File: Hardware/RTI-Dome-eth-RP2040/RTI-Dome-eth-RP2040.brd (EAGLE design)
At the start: 106.7 x 71.2 mm, 112 parts, among them IC1 RP2040, IC2 24LC128T-I_SN, IC3 FT232RL, IC5 74LVC245, IC6 74ABT245, IC7 W25Q128JVSIM_TR, IC8 REG1117-3.3V, IC9 REG1117-5V, J1 47642-1001, J2 XT60PW-M, U1 W5500, X13 PN61729-S, X9 J1011F21PNL

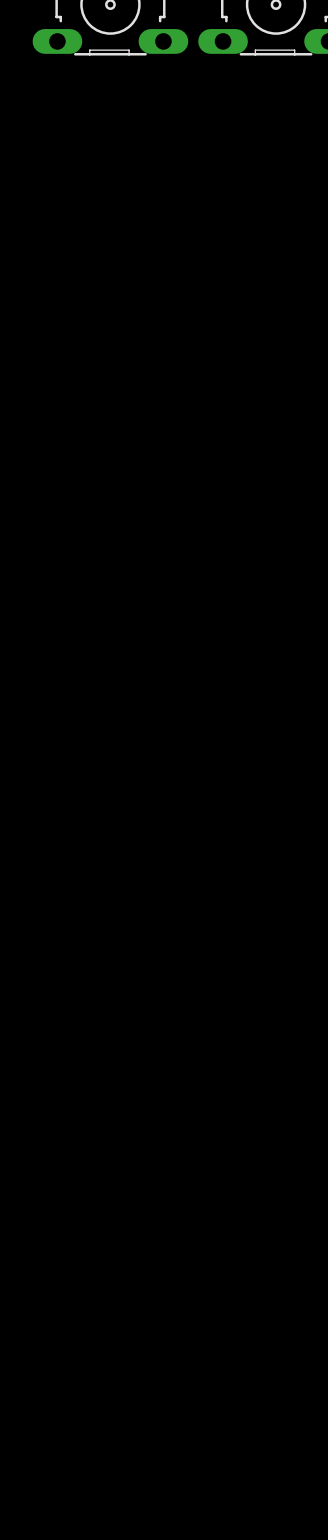
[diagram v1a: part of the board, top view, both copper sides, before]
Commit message: Some addition small fixes to Firmware on RP2040. Tested and working.
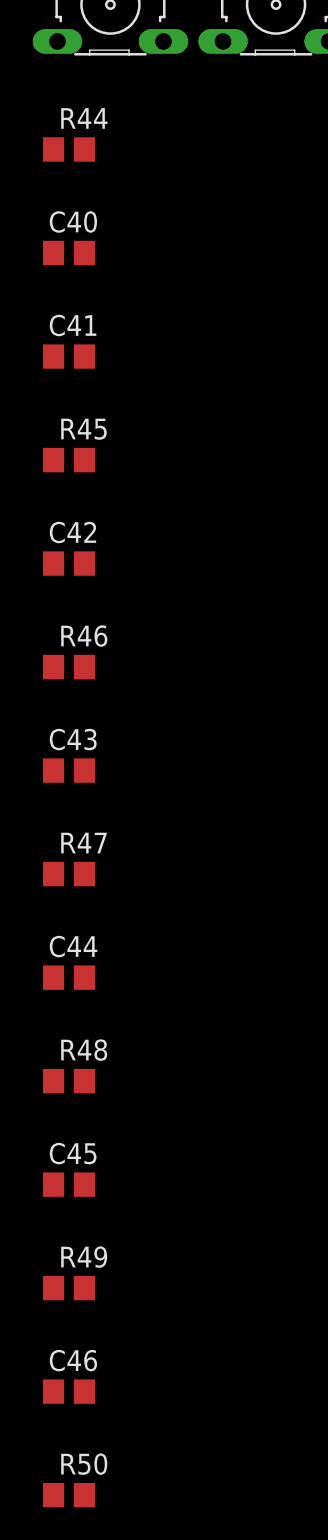
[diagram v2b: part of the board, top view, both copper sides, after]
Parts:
- added C40, C41, C42, C43, C44, C45, C46: 10uF, rcl:C0805
- added R44, R45, R46, R47, R48, R49, R50: 100, rcl:R0805
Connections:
- removed net AT_PARK_PIN_EXT: IC5.P$9, R20.1, X7.2
- removed net BUTTON_WEST_CLOSE_5V: IC5.P$4, R15.2, X4.3
- removed net HOME_SHUTTER_CLOSED_5V: IC5.P$3, R18.2, X1.2
- removed net SHUTTER_OPENED_5V: IC5.P$8, R17.2, X3.2
- removed net SPARE1_EXT: IC5.P$2, R21.2, X8.1
- removed net SPARE2_EXT: IC5.P$6, R9.2, X8.2
- new net AT_PARK_PIN-IN_EXT: R46.2, X7.2
- new net AT_PARK_PIN_IN_5V: C42.1, IC5.P$9, R20.1, R46.1
- new net BUTTON_EAST_OPEN-IN_EXT: R44.2, X4.2
- new net BUTTON_WEST_CLOSE-IN_EXT: R47.2, X4.3
- new net BUTTON_WEST_CLOSE_IN_5V: C43.1, IC5.P$4, R15.2, R47.1
- new net HOME_SHUTTER_CLOSED-IN_EXT: R50.2, X1.2
- new net HOME_SHUTTER_CLOSED_IN_5V: C46.1, IC5.P$3, R18.2, R50.1
- new net SHUTTER_OPENED-IN_EXT: R48.2, X3.2
- new net SHUTTER_OPENED_IN_5V: C44.1, IC5.P$8, R17.2, R48.1
- new net SPARE1-IN_EXT: R45.2, X8.1
- new net SPARE1_IN_5V: C41.1, IC5.P$2, R21.2, R45.1
- new net SPARE2-IN_EXT: R49.2, X8.2
- new net SPARE2_IN_5V: C45.1, IC5.P$6, R49.1, R9.2
- net BUTTON_EAST_OPEN_5V: now also C40.1, R44.1; no longer X4.2
- net GND: now also C40.2, C41.2, C42.2, C43.2, C44.2, C45.2, C46.2

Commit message: Set the shuuter response to open when there is no shutter controler
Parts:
- removed 12MHZ: CB3LV-OSCILATOR, rti:SMD-7050_4P
- removed BOOT_SEL: (no value), switch-omron:B3F-10XX
- removed C25, C26, C29, C30, C31, C32, C33, C34, C35, C37, C38: 100nF, rcl:C0805
- removed C36, C39: 2.2uF, rcl:C0805
- removed IC1: RP2040, samacsys:QFN40P700X700X90-57N
- removed IC7: W25Q128JVSIM_TR, samacsys:SOIC127P790X216-8N
- removed J1: 47642-1001, samacsys:476421001
- removed R22, R41: 27.4, rcl:R0805
- removed R42: 10K, rcl:R0805
- removed R43: 1k, rcl:R0805
- added IC4: RASPBERRY_PI_PICO, samacsys:RASPBERRYPIPICOW
- moved R50 276.3 mm to (64.8, 64.8), turned to 180 degrees
- moved C46 271.7 mm to (69.2, 64.8)
- moved R49 255.3 mm to (29.2, 64.8), turned to 180 degrees
- moved C45 250.0 mm to (33.7, 64.8)
- moved R48 249.4 mm to (55.9, 64.8), turned to 180 degrees
- moved C44 244.8 mm to (60.3, 64.8)
- moved R47 243.5 mm to (73.7, 64.8), turned to 180 degrees
- moved R46 241.5 mm to (95.9, 64.8), turned to 180 degrees
- moved C43 239.4 mm to (78.1, 64.8)
- moved C42 238.1 mm to (100.3, 64.8)
- moved C40 214.9 mm to (87.0, 64.8)
- moved R45 207.9 mm to (38.1, 64.8), turned to 180 degrees
- moved R44 207.2 mm to (82.5, 64.8), turned to 180 degrees
- moved C41 203.0 mm to (42.5, 64.8)
- moved RESET 134.7 mm to (58.4, 5.08), turned to 90 degrees
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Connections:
- net USBDM renamed USBD_N
- net USBDP renamed USBD_P
- removed net $N38: IC1.35
- removed net 1.1V: C37.1, C38.1, C39.1, IC1.23, IC1.45, IC1.50
- removed net CLOCK_IN: 12MHZ.3, IC1.20
- removed net N$1: IC1.36
- removed net N$14: J1.3, R22.2
- removed net N$16: BOOT_SEL.1, BOOT_SEL.2, R43.1
- removed net N$39: IC1.37
- removed net N$4: J1.2, R41.2
- removed net N$40: IC1.39
- removed net N$42: IC1.41
- removed net QSPI_CS: IC1.56, IC7.1, R42.2, R43.2
- removed net QSPI_SCLK: IC1.52, IC7.6
- removed net QSPI_SD0: IC1.53, IC7.5
- removed net QSPI_SD1: IC1.55, IC7.2
- removed net QSPI_SD2: IC1.54, IC7.3
- removed net QSPI_SD3: IC1.51, IC7.7
- removed net USB_DM: IC1.46, R41.1
- removed net USB_DP: IC1.47, R22.1
- new net N$56: IC4.32
- new net N$59: IC4.35
- new net N$60: IC4.36
- new net N$61: IC4.37
- new net N$64: IC4.40
- net 3.3V: no longer 12MHZ.1, 12MHZ.4, C25.1, C26.1, C29.1, C30.1, C31.1, C32.1, C33.1, C34.1, C35.1, C36.1, IC1.1, IC1.10, IC1.22, IC1.33, IC1.42, IC1.43, IC1.44, IC1.48, IC1.49, IC7.8, R42.1
- net AT_PARK_PIN: now also IC4.20; no longer IC1.18
- net BUTTON_EAST_OPEN: now also IC4.15; no longer IC1.14
- net BUTTON_WEST_CLOSE: now also IC4.14; no longer IC1.13
- net ETH_CS: now also IC4.22; no longer IC1.28
- net ETH_RESET: now also IC4.26; no longer IC1.31
- net FTDI_RESET: now also IC4.34; no longer IC1.40
- net GND: now also IC4.13, IC4.18, IC4.23, IC4.28, IC4.3, IC4.33, IC4.38, IC4.8; no longer 12MHZ.2, BOOT_SEL.3, BOOT_SEL.4, C25.2, C26.2, C29.2, C30.2, C31.2, C32.2, C33.2, C34.2, C35.2, C36.2, C37.2, C38.2, C39.2, IC1.57, IC7.4, J1.5, J1.MH1, J1.MH2, J1.MH3, J1.MH4
- net HOME_SHUTTER_CLOSED: now also IC4.10; no longer IC1.9
- net M_DIR: now also IC4.5; no longer IC1.5
- net M_EN: now also IC4.4; no longer IC1.4
- net M_STEP: now also IC4.27; no longer IC1.32
- net RESET: now also IC4.30; no longer IC1.26
- net RG-11: now also IC4.17; no longer IC1.16
- net RX2: now also IC4.12; no longer IC1.12
- net SCL: now also IC4.7; no longer IC1.7
- net SCLK: now also IC4.24; no longer IC1.29
- net SDA: now also IC4.6; no longer IC1.6
- net SDI: now also IC4.21; no longer IC1.27
- net SDO: now also IC4.25; no longer IC1.30
- net SHUTTER_OPENED: now also IC4.19; no longer IC1.17
- net SPARE1: now also IC4.9; no longer IC1.8
- net SPARE2: now also IC4.16; no longer IC1.15
- net TX2: now also IC4.11; no longer IC1.11
- net VCC: now also IC4.39
- net VPIN: now also IC4.31; no longer IC1.38
- net XBEE_DIN: now also IC4.1; no longer IC1.2
- net XBEE_DOUT: now also IC4.2; no longer IC1.3
- net XBEE_RESET: now also IC4.29; no longer IC1.34
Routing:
- net VCC: track 0.00 -> 232.3 mm, vias 0 -> 5
- net 3.3V: track 0.00 -> 204.4 mm, vias 0 -> 6
- net +12V: track 0.00 -> 154.9 mm
- net M_STEP: track 0.00 -> 74.0 mm
- net AVDD: track 0.00 -> 67.6 mm
- net XBEE_DIN: track 0.00 -> 46.1 mm
- net M_EN: track 0.00 -> 45.7 mm
- net ETH_RESET: track 0.00 -> 44.1 mm, vias 0 -> 2
- net M_DIR: track 0.00 -> 42.9 mm
- net XBEE_DOUT: track 0.00 -> 40.4 mm
- net TXN: track 0.00 -> 39.2 mm, vias 0 -> 1
- net LINK_ACK: track 0.00 -> 37.7 mm, vias 0 -> 1
- net TXP: track 0.00 -> 37.4 mm, vias 0 -> 1
- net ACT_LED: track 0.00 -> 36.5 mm, vias 0 -> 2
- net SCLK: track 0.00 -> 36.0 mm, vias 0 -> 2
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- removed copper zone on layer 1, net 3.3V
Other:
- board size 106.7 x 71.2 mm -> 111.1 x 76.3 mm

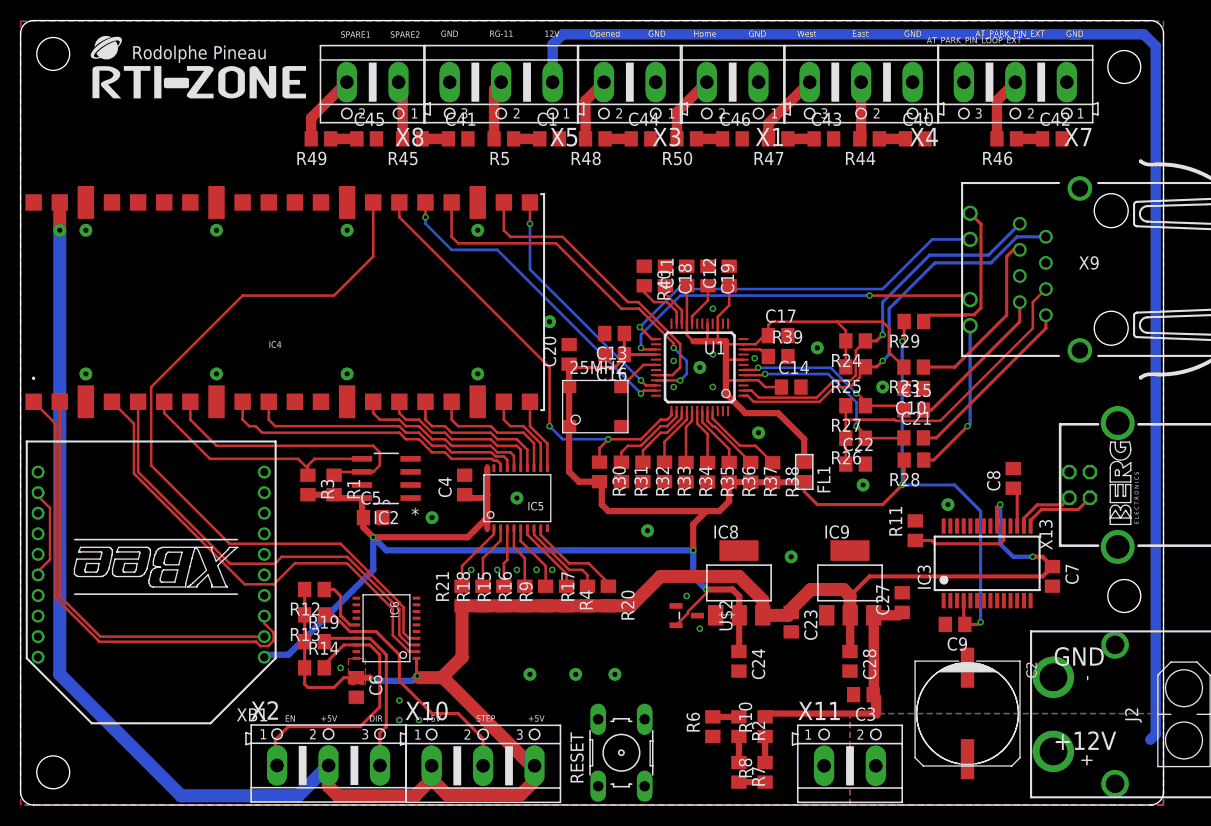
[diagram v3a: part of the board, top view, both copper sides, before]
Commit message: Finished routing on RP2040 board
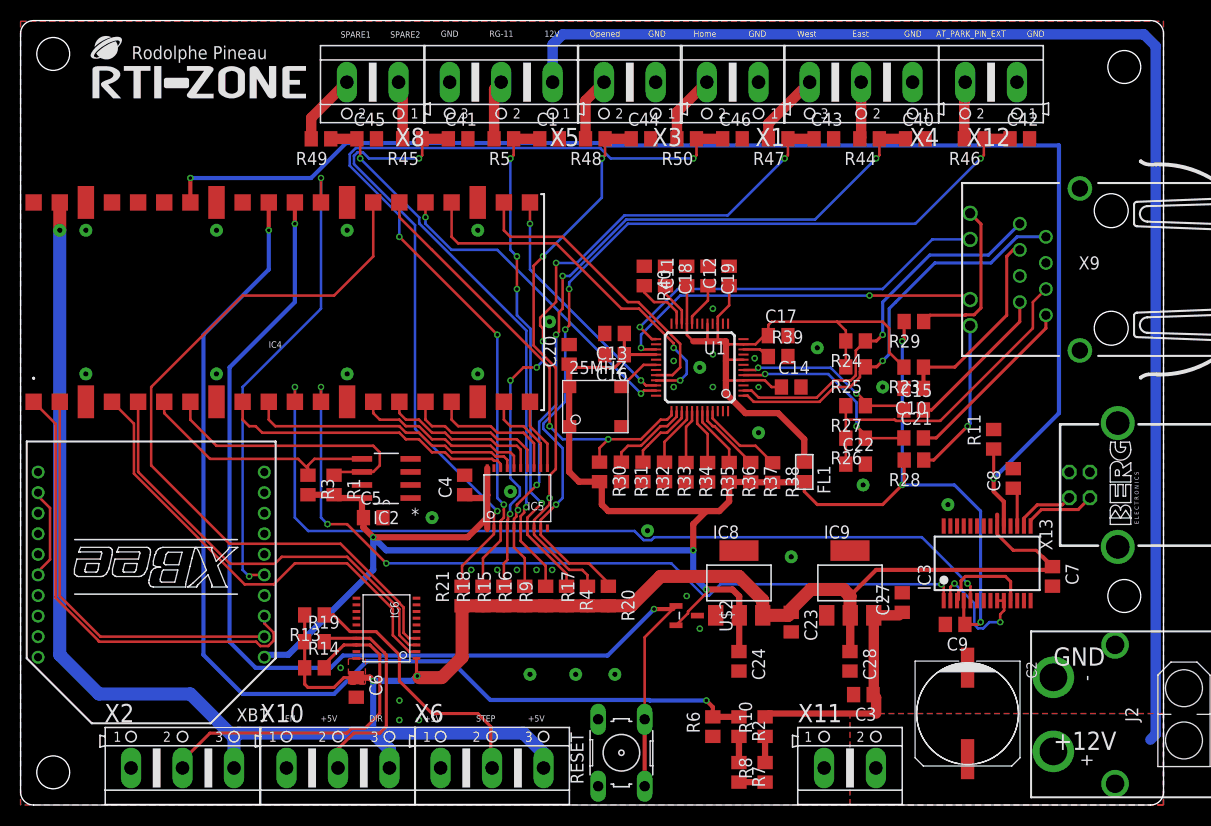
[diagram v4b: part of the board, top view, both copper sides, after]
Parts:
- removed R12: 4.7K, rcl:R0805
- removed X7: (no value), rti:AK500/3
- added X12: (no value), rti:AK500/2
- added X6: (no value), rti:AK500/3
- moved X2 14.2 mm to (15.7, 3.60)
- moved X10 14.1 mm to (30.9, 3.60)
- moved R11 11.7 mm to (94.6, 35.6)
- moved R46 3.18 mm to (92.7, 64.8)
- moved C42 3.17 mm to (97.2, 64.8)
- moved X11 0.21 mm to (80.6, 3.60)
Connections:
- net AT_PARK_PIN-IN_EXT: now also X12.2; no longer X7.2
- net AT_PARK_PIN_LOOP_EXT: no longer R12.1, X7.3
- net GND: now also X10.1, X12.1, X2.1, X6.1; no longer X7.1
- net M_DIR_5V: now also X10.2; no longer X2.3
- net M_EN_5V: now also X2.2; no longer X2.1
- net M_STEP_5V: now also X6.2; no longer X10.2
- net VCC: now also X2.3, X6.3; no longer R12.2, X10.1, X2.2
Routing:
- net FTDI_RESET: track 10.3 -> 131.2 mm, vias 0 -> 2
- net RESET: track 0.00 -> 111.1 mm, vias 0 -> 2
- net VPIN: track 2.54 -> 104.4 mm, vias 0 -> 2
- net TX2: track 0.00 -> 84.2 mm, vias 0 -> 2
- net RX2: track 0.00 -> 79.8 mm, vias 0 -> 4
- net HOME_SHUTTER_CLOSED_IN_5V: track 8.89 -> 87.7 mm, vias 0 -> 4
- net AT_PARK_PIN_IN_5V: track 12.0 -> 85.7 mm, vias 0 -> 4
- net BUTTON_EAST_OPEN_5V: track 8.61 -> 72.5 mm, vias 0 -> 5
- net BUTTON_WEST_CLOSE_IN_5V: track 8.32 -> 66.4 mm, vias 0 -> 6
- net SPARE1_IN_5V: track 9.46 -> 60.3 mm, vias 0 -> 2
- net XBEE_RESET: track 0.00 -> 46.1 mm, vias 0 -> 2
- net SPARE2_IN_5V: track 9.19 -> 54.1 mm, vias 0 -> 2
- net SHUTTER_OPENED_IN_5V: track 11.1 -> 53.6 mm, vias 0 -> 3
- net RG-11-IN_5V: track 9.76 -> 49.6 mm, vias 0 -> 4
- net VCC: track 232.3 -> 216.7 mm, vias 5 -> 3
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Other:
- board text removed: "AT_PARK_PIN_LOOP_EXT"

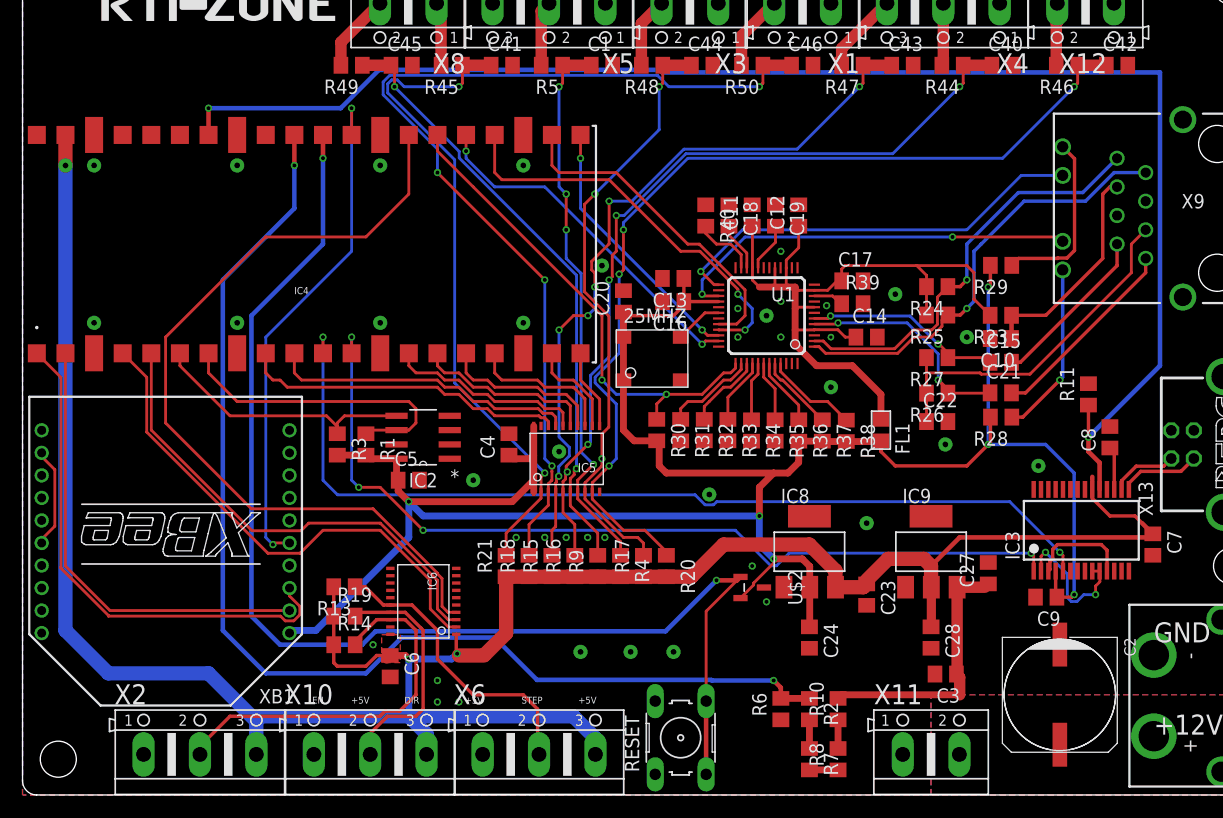
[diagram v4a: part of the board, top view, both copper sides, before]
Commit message: moved some component to avoid colisions (3D rendring helps ! )
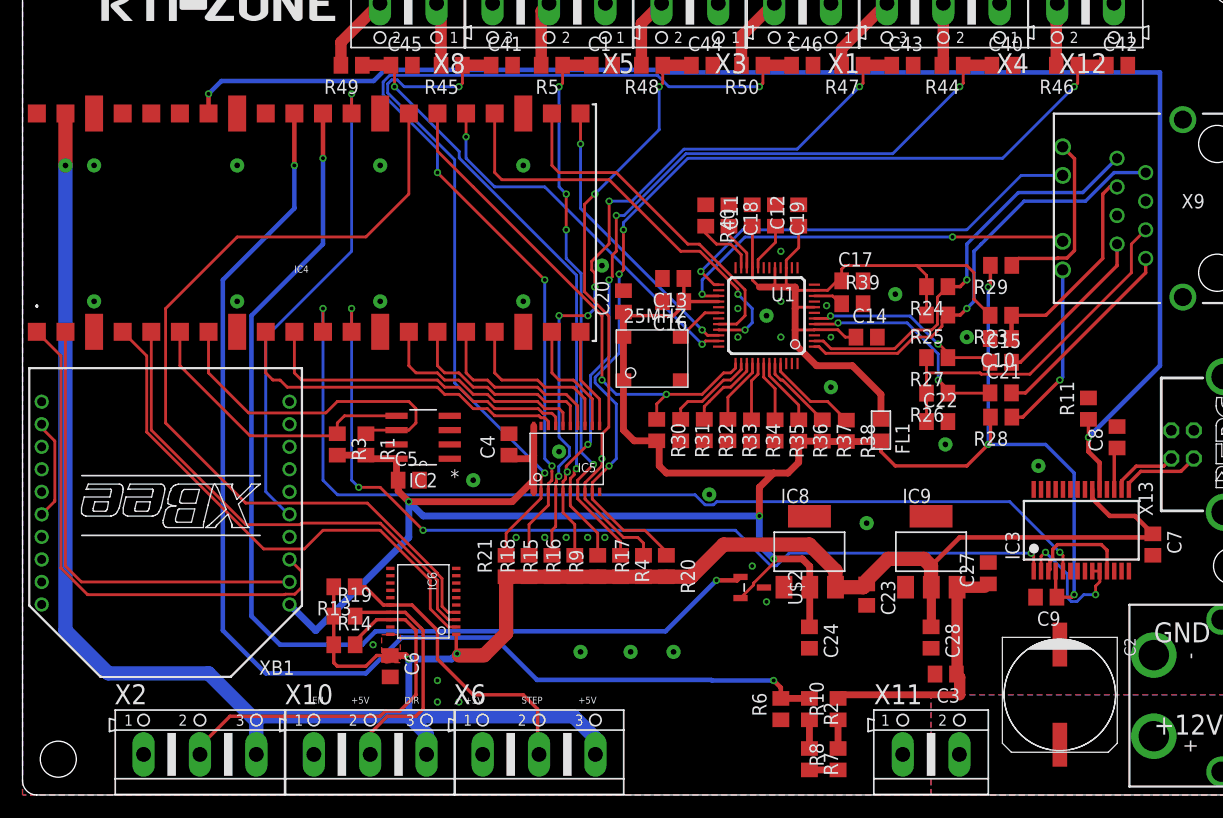
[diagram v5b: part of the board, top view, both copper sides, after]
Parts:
- removed RESET: (no value), switch-omron:B3F-10XX
- moved XB1 2.54 mm to (12.7, 25.9)
- moved IC4 1.90 mm to (25.4, 50.8)
- moved R11 1.27 mm to (94.6, 34.3)
- moved C8 0.64 mm to (97.2, 31.8)
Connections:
- net GND: no longer RESET.1, RESET.2
- net RESET: no longer RESET.3, RESET.4
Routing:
- net RESET: track 111.1 -> 94.2 mm
- net M_STEP: track 74.0 -> 77.4 mm
- net TX2: track 84.2 -> 87.4 mm
- net RX2: track 79.8 -> 82.9 mm
- net XBEE_RESET: track 46.1 -> 43.1 mm, vias 2 -> 1
- net SCL: track 27.6 -> 30.3 mm
- net FTDI_RESET: track 131.2 -> 128.8 mm
- net VPIN: track 104.4 -> 106.3 mm
- net SPARE1: track 29.0 -> 30.9 mm
- net SHUTTER_OPENED: track 8.68 -> 10.6 mm
- net SDO: track 31.4 -> 33.4 mm
- net SDI: track 23.4 -> 25.4 mm
- net SCLK: track 36.0 -> 37.9 mm
- net RG-11: track 13.1 -> 15.0 mm
- net HOME_SHUTTER_CLOSED: track 27.4 -> 29.3 mm
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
